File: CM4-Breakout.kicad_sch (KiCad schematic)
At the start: 2 parts

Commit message: Some work was done
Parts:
- removed Module? (x2): ComputeModule4-CM4, CM4IO:Raspberry-Pi-4-Compute-Module, symbol CM4IO:ComputeModule4-CM4
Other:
- added sheet CM4_ModuleA (CM4_ModuleA.kicad_sch)
- added sheet CM4_ModuleB (CM4_ModuleB.kicad_sch)
- added sheet Pinout (Pinout.kicad_sch)

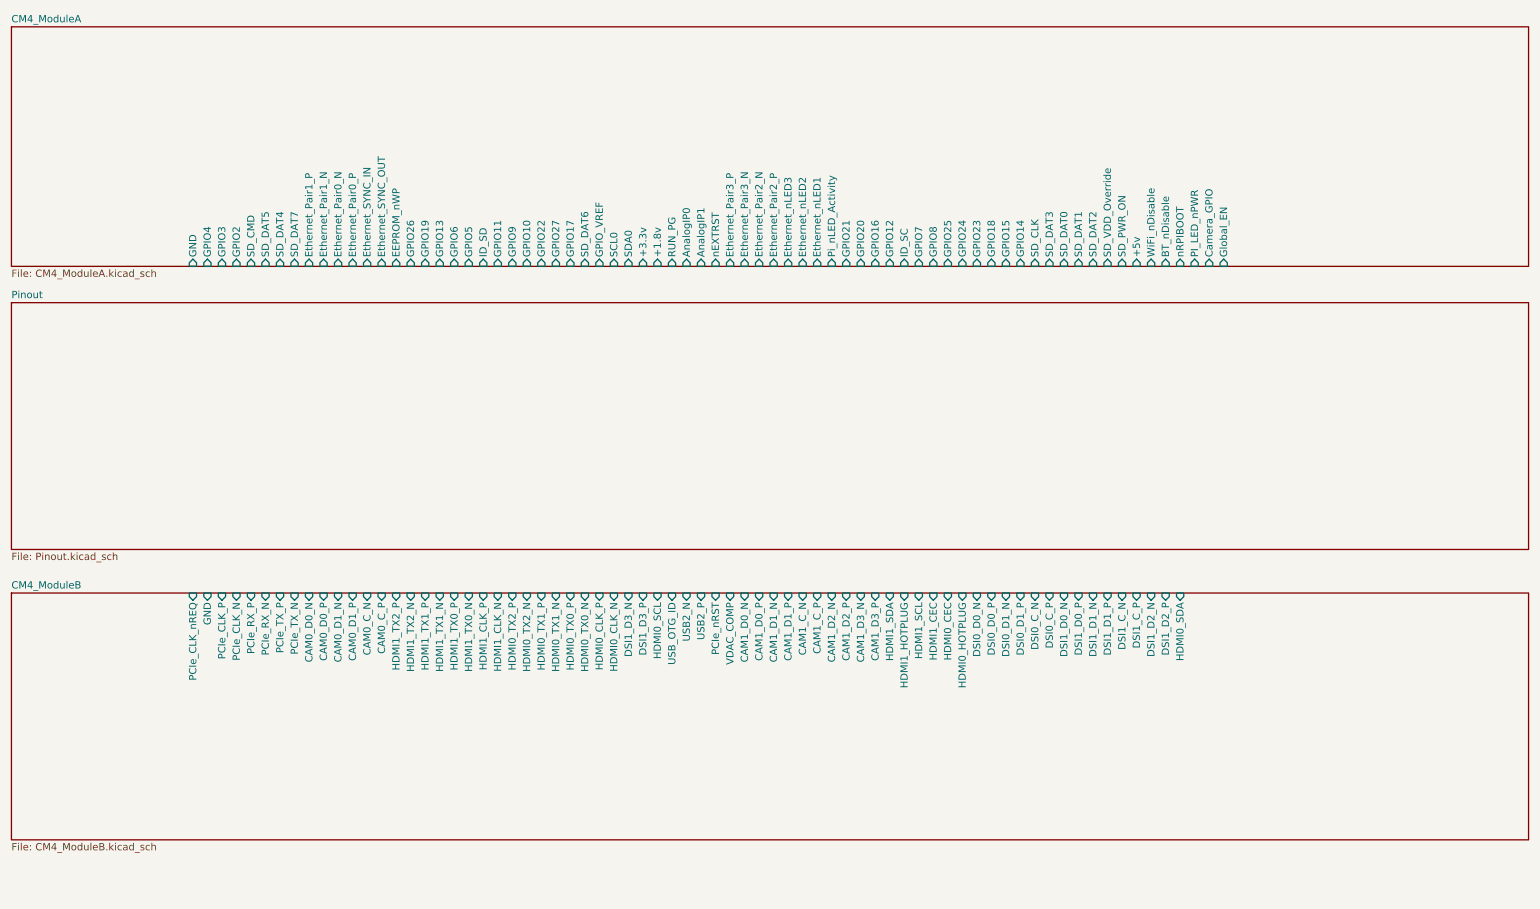
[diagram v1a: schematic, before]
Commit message: PCB ready to trace
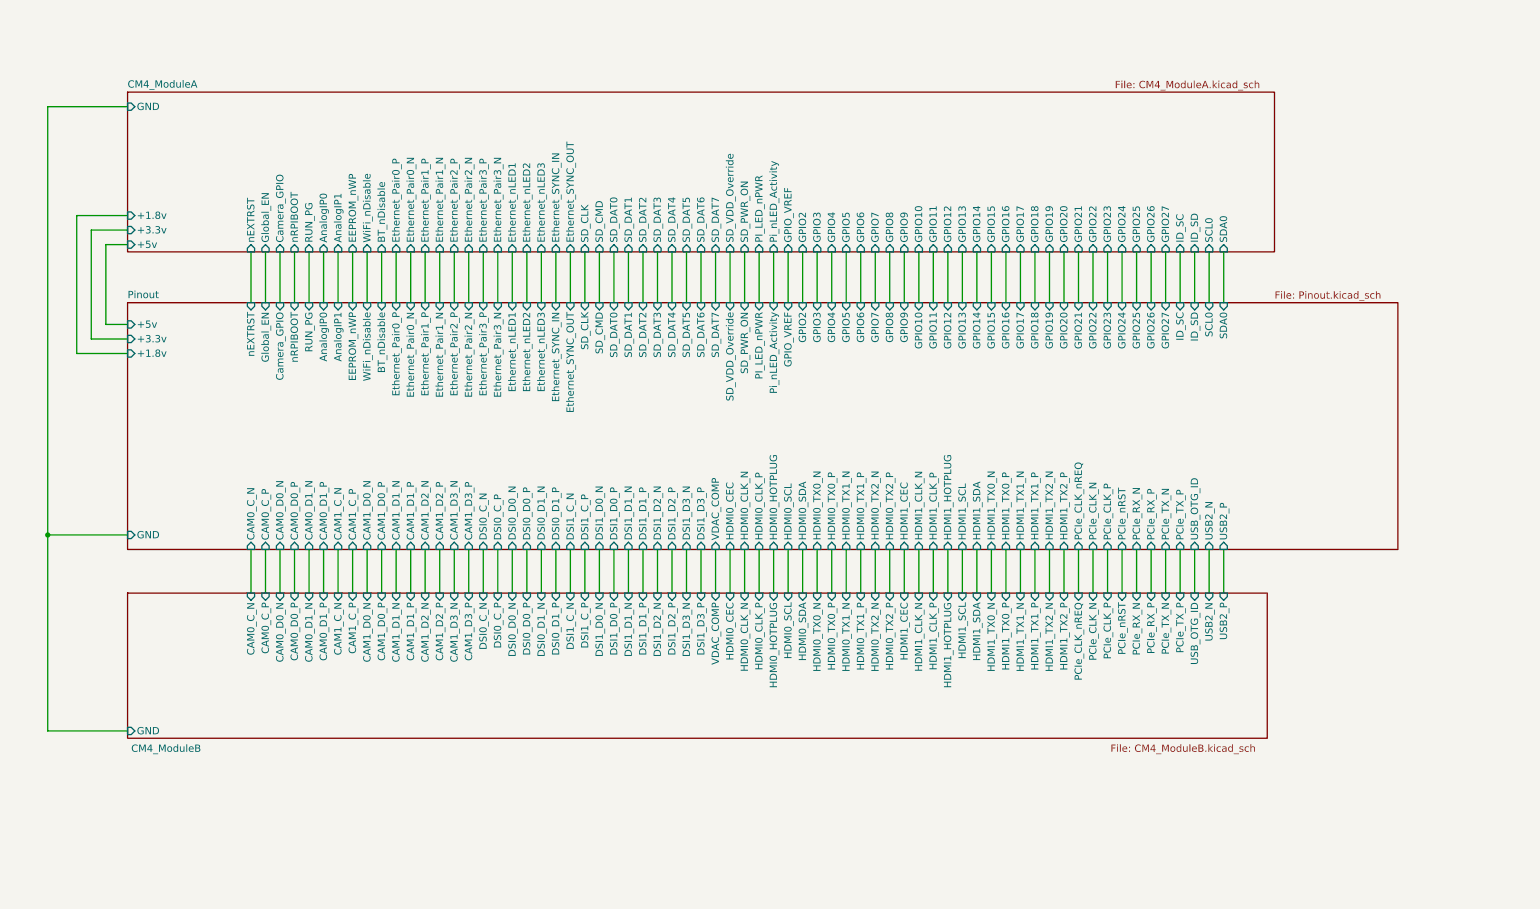
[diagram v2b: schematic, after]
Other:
- sheet Pinout ports: added +1.8v, +3.3v, +5v, AnalogIP0, AnalogIP1, BT_nDisable, CAM0_C_N, CAM0_C_P, CAM0_D0_N, CAM0_D0_P, CAM0_D1_N, CAM0_D1_P, CAM1_C_N, CAM1_C_P, CAM1_D0_N, CAM1_D0_P, CAM1_D1_N, CAM1_D1_P, CAM1_D2_N, CAM1_D2_P, CAM1_D3_N, CAM1_D3_P, Camera_GPIO, DSI0_C_N, DSI0_C_P, DSI0_D0_N, DSI0_D0_P, DSI0_D1_N, DSI0_D1_P, DSI1_C_N, DSI1_C_P, DSI1_D0_N, DSI1_D0_P, DSI1_D1_N, DSI1_D1_P, DSI1_D2_N, DSI1_D2_P, DSI1_D3_N, DSI1_D3_P, EEPROM_nWP, Ethernet_Pair0_N, Ethernet_Pair0_P, Ethernet_Pair1_N, Ethernet_Pair1_P, Ethernet_Pair2_N, Ethernet_Pair2_P, Ethernet_Pair3_N, Ethernet_Pair3_P, Ethernet_SYNC_IN, Ethernet_SYNC_OUT, Ethernet_nLED1, Ethernet_nLED2, Ethernet_nLED3, GND, GPIO10, GPIO11, GPIO12, GPIO13, GPIO14, GPIO15, GPIO16, GPIO17, GPIO18, GPIO19, GPIO2, GPIO20, GPIO21, GPIO22, GPIO23, GPIO24, GPIO25, GPIO26, GPIO27, GPIO3, GPIO4, GPIO5, GPIO6, GPIO7, GPIO8, GPIO9, GPIO_VREF, Global_EN, HDMI0_CEC, HDMI0_CLK_N, HDMI0_CLK_P, HDMI0_HOTPLUG, HDMI0_SCL, HDMI0_SDA, HDMI0_TX0_N, HDMI0_TX0_P, HDMI0_TX1_N, HDMI0_TX1_P, HDMI0_TX2_N, HDMI0_TX2_P, HDMI1_CEC, HDMI1_CLK_N, HDMI1_CLK_P, HDMI1_HOTPLUG, HDMI1_SCL, HDMI1_SDA, HDMI1_TX0_N, HDMI1_TX0_P, HDMI1_TX1_N, HDMI1_TX1_P, HDMI1_TX2_N, HDMI1_TX2_P, ID_SC, ID_SD, PCIe_CLK_N, PCIe_CLK_P, PCIe_CLK_nREQ, PCIe_RX_N, PCIe_RX_P, PCIe_TX_N, PCIe_TX_P, PCIe_nRST, PI_LED_nPWR, Pi_nLED_Activity, RUN_PG, SCL0, SDA0, SD_CLK, SD_CMD, SD_DAT0, SD_DAT1, SD_DAT2, SD_DAT3, SD_DAT4, SD_DAT5, SD_DAT6, SD_DAT7, SD_PWR_ON, SD_VDD_Override, USB2_N, USB2_P, USB_OTG_ID, VDAC_COMP, WiFi_nDisable, nEXTRST, nRPIBOOT; removed none
